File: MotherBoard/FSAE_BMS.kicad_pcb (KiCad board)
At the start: 2 copper layers, 203 parts, among them IC501 BQ79600PWRQ1, J201 Conn_ARM_SWD_TagConnect_TC2030, J202 DM3AT-SF-PEJM5_40_, J301 1376357-3, J302 Conn_01x04_Pin, J303 430450200, Q701 Q_NMOS_GDS, Q702 Q_NPN_BEC, Q703 Q_NPN_BEC, Q704 Q_NMOS_GDS, Q705 Q_NPN_BEC, Q706 Q_NMOS_GDS, Q708 Q_NPN_BEC, Q709 Q_NMOS_GDS, U201 STM32F205RBTx, U401 LMR51430, U402 LMR51430, U601 PTCAN1462DRQ1, U602 PTCAN1462DRQ1, Y201 16 Mhz

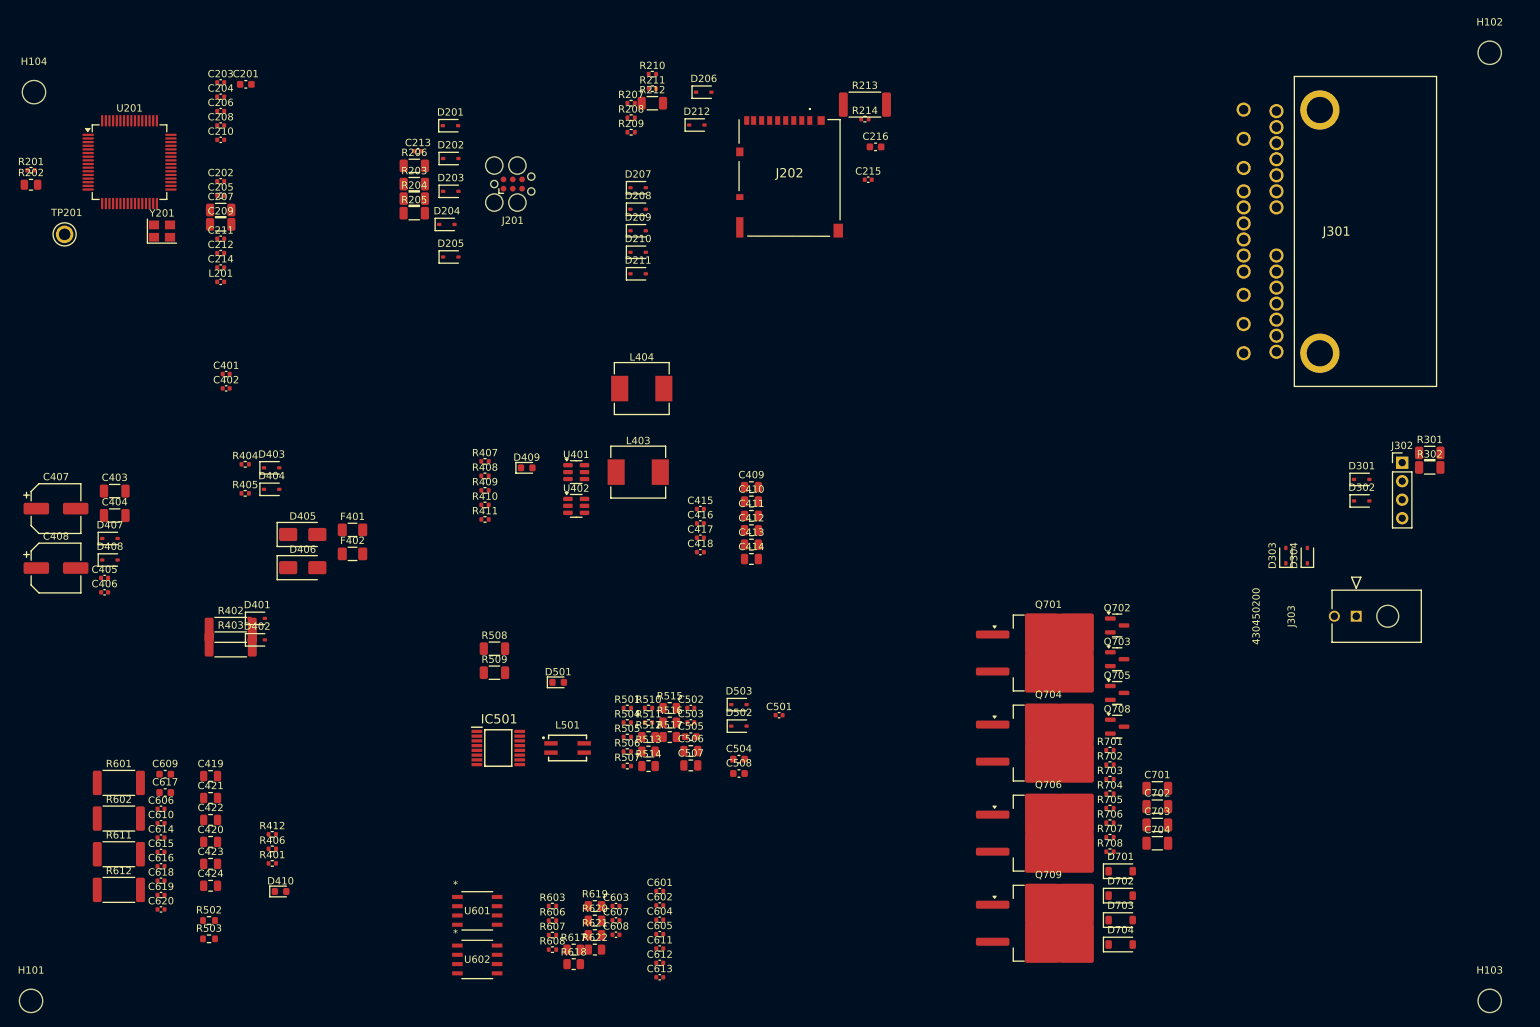
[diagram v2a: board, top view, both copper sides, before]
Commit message: BOM completed + All 3D models added + Initial board shape complete
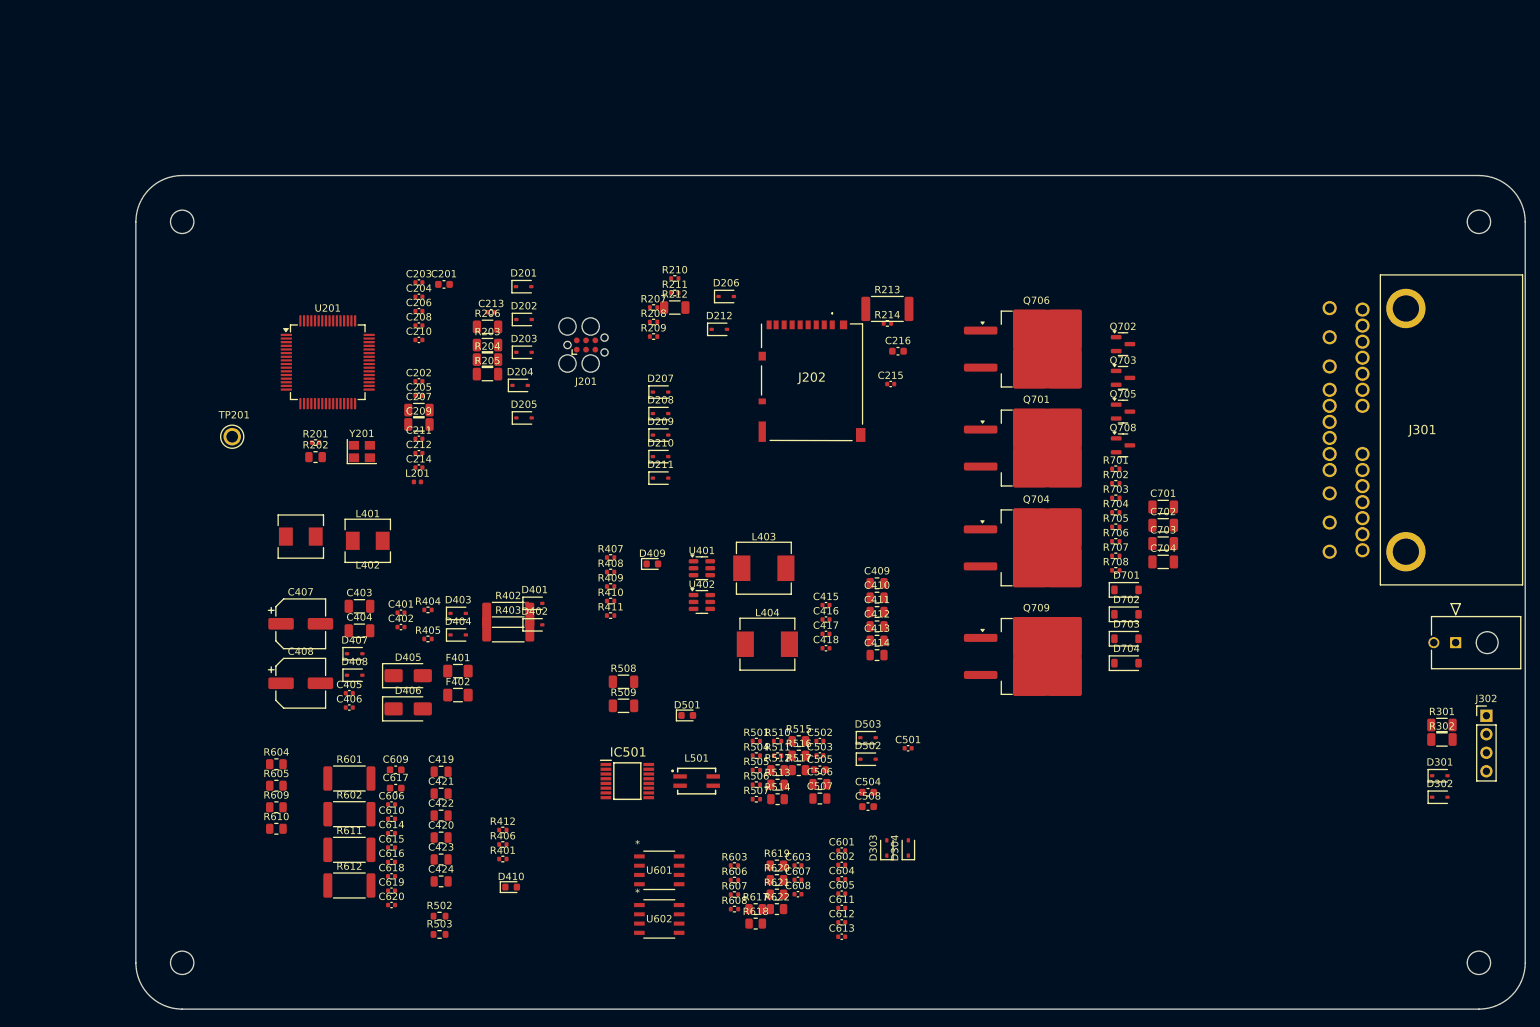
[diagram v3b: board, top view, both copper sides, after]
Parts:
- added L401: 1.2u, Inductor_SMD:L_Chilisin_BMRA00050530, F.Cu at (71.2, 86.9)
- added L402: 1.2u, Inductor_SMD:L_Chilisin_BMRA00050530, F.Cu at (62.0, 86.3)
- added R604: 0R, Resistor_SMD:R_0805_2012Metric, F.Cu at (58.6, 117.5)
- added R605: 0R, Resistor_SMD:R_0805_2012Metric, F.Cu at (58.6, 120.5)
- added R609: 0R, Resistor_SMD:R_0805_2012Metric, F.Cu at (58.6, 123.4)
- added R610: 0R, Resistor_SMD:R_0805_2012Metric, F.Cu at (58.6, 126.4)
- L201: footprint Capacitor_SMD:C_0402_1005Metric -> Inductor_SMD:L_0402_1005Metric
- moved H101 198.6 mm to (223.5, 144.8)
- moved H102 180.8 mm to (45.7, 43.2)
- moved H104 121.1 mm to (45.7, 144.8)
- moved H103 106.8 mm to (223.5, 43.2)
- moved D303 67.8 mm to (142.3, 129.0)
- moved D304 67.8 mm to (145.3, 129.0)
- moved Q706 66.4 mm to (162.9, 60.6)
- moved R201 54.0 mm to (64.0, 73.4)
- moved R202 54.0 mm to (64.0, 75.4)
- moved D301 42.0 mm to (218.2, 119.1)
- moved D302 42.0 mm to (218.2, 122.1)
- moved Y201 40.8 mm to (70.4, 74.7)
- moved C401 40.6 mm to (75.7, 96.8)
- moved C402 40.6 mm to (75.7, 98.7)
- moved L404 39.1 mm to (126.0, 101.1)
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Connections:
- U601 pad 6: ISO_CAN1- -> /TCAN1462-Q1/CANL_1
- U601 pad 7: ISO_CAN1+ -> /TCAN1462-Q1/CANH_1
- U602 pad 6: ISO_CAN2- -> /TCAN1462-Q1/CANL_2
- U602 pad 7: ISO_CAN2+ -> /TCAN1462-Q1/CANH_2
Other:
- board outline added: 190.5 x 114.3 mm

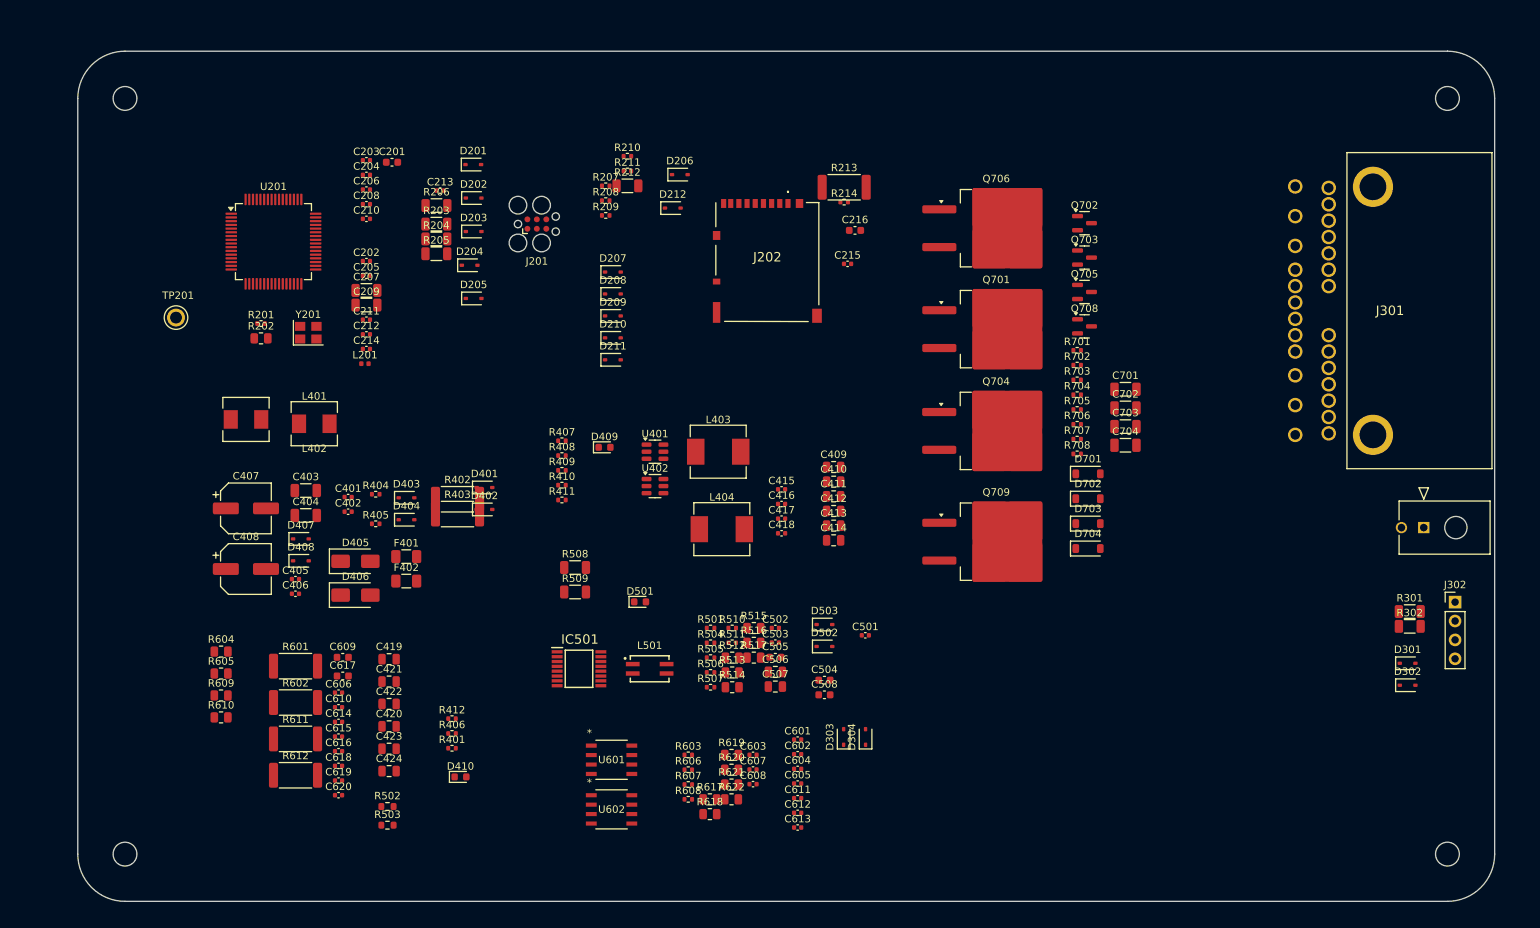
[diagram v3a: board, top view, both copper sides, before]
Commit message: Finished MCU + Tranceiver layout
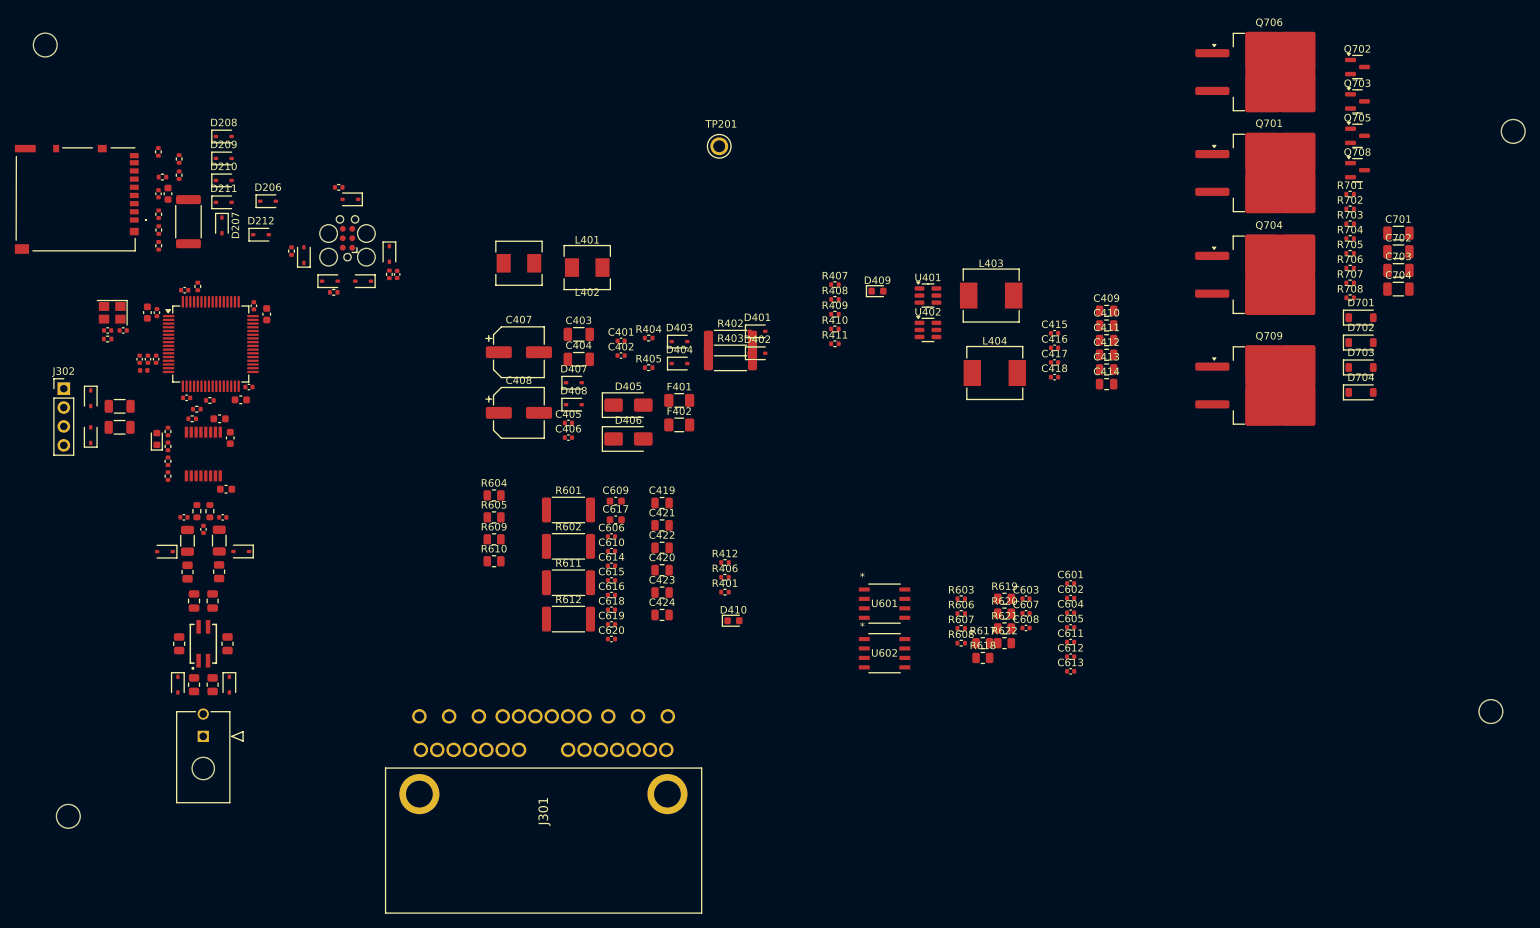
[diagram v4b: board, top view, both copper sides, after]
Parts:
- C207, C209: footprint Resistor_SMD:R_1206_3216Metric -> Capacitor_SMD:C_0603_1608Metric
- R202: footprint Resistor_SMD:R_0805_2012Metric -> Resistor_SMD:R_0402_1005Metric
- R203, R204, R205, R206, R212: footprint Resistor_SMD:R_1206_3216Metric -> Resistor_SMD:R_0402_1005Metric
- moved J302 189.2 mm to (37.5, 82.2)
- moved H103 188.7 mm to (35.0, 36.0)
- moved H102 186.7 mm to (232.4, 47.6)
- moved H101 185.5 mm to (38.1, 139.7)
- moved H104 184.6 mm to (229.4, 125.6)
- moved D302 181.2 mm to (41.1, 83.5), turned to -90 degrees
- moved D301 179.7 mm to (41.1, 88.5), turned to 90 degrees
- moved R301 175.6 mm to (45.0, 84.6)
- moved R302 175.5 mm to (45.0, 87.4)
- moved J303 166.5 mm to (56.2, 129.0), turned to 0 degrees
- moved J301 110.4 mm to (118.7, 126.3), turned to -90 degrees
- moved C215 93.1 mm to (50.2, 56.0), turned to 90 degrees
- moved C216 92.5 mm to (51.5, 56.0), turned to 90 degrees
- moved R214 92.5 mm to (50.2, 50.4), turned to -90 degrees
- moved C501 90.1 mm to (56.3, 101.1), turned to 90 degrees
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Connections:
- R203 pad 1: /MCU/CONN_NRST -> /MCU/CONN_SWDIO
- R203 pad 2: /MCU/NRST -> /MCU/SWDIO
- R205 pad 1: /MCU/CONN_SWDIO -> /MCU/CONN_NRST
- R205 pad 2: /MCU/SWDIO -> /MCU/NRST
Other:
- board outline removed
- copper layers 2 -> 4

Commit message: Layout 90% complete
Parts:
- R601, R602, R611, R612: footprint Resistor_SMD:R_2512_6332Metric -> Resistor_SMD:R_1210_3225Metric
- R604, R605, R609, R610: footprint Resistor_SMD:R_0805_2012Metric -> Resistor_SMD:R_1206_3216Metric
- moved H103 208.1 mm to (210.8, 147.3)
- moved J302 159.9 mm to (188.2, 28.9), turned to -90 degrees
- moved D302 154.4 mm to (186.9, 32.5), turned to 180 degrees
- moved J202 153.1 mm to (199.1, 70.1), turned to 90 degrees
- moved H102 152.1 mm to (81.3, 30.5)
- moved D301 151.5 mm to (181.9, 32.5), turned to 0 degrees
- moved R301 148.8 mm to (185.8, 36.4), turned to -90 degrees
- moved R302 147.1 mm to (183.0, 36.4), turned to -90 degrees
- moved J303 146.4 mm to (166.0, 32.0), turned to 180 degrees
- moved R214 145.2 mm to (192.1, 81.1), turned to 90 degrees
- moved C215 143.2 mm to (192.1, 75.4), turned to -90 degrees
- moved R212 142.8 mm to (191.6, 77.7), turned to 0 degrees
- moved R209 142.5 mm to (192.1, 72.7), turned to -90 degrees
- moved R208 142.1 mm to (192.0, 70.6), turned to -90 degrees
- moved R207 141.9 mm to (192.1, 68.4), turned to -90 degrees
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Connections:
- R601 pad 1: Net-(C606-Pad1) -> Net-(C603-Pad1)
- R601 pad 2: ISO_CAN2+ -> ISO_CAN1+
- R602 pad 1: ISO_CAN2- -> ISO_CAN1-
- R602 pad 2: Net-(C606-Pad1) -> Net-(C603-Pad1)
- R604 pad 1: /TCAN1462-Q1/CANL_2 -> /TCAN1462-Q1/CANL_1
- R604 pad 2: ISO_CAN2- -> ISO_CAN1-
- R610 pad 1: /TCAN1462-Q1/CANL_1 -> /TCAN1462-Q1/CANL_2
- R610 pad 2: ISO_CAN1- -> ISO_CAN2-
- R611 pad 1: Net-(C603-Pad1) -> Net-(C606-Pad1)
- R611 pad 2: ISO_CAN1+ -> ISO_CAN2+
- R612 pad 1: ISO_CAN1- -> ISO_CAN2-
- R612 pad 2: Net-(C603-Pad1) -> Net-(C606-Pad1)
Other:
- board outline added: 139.7 x 127 mm
